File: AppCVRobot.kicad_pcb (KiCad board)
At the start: 2 copper layers, 34 parts, among them U1 LevelShifter

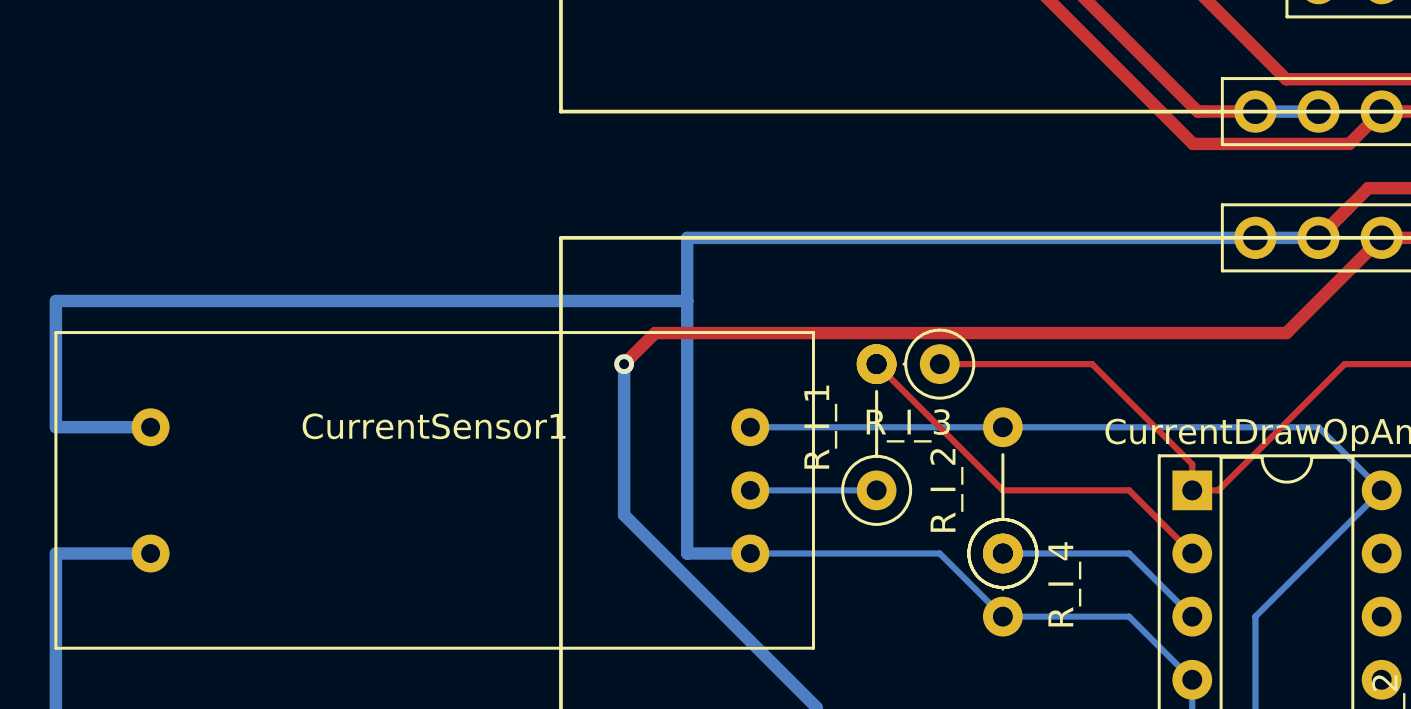
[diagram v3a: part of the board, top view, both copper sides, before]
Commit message: Added power switch connector
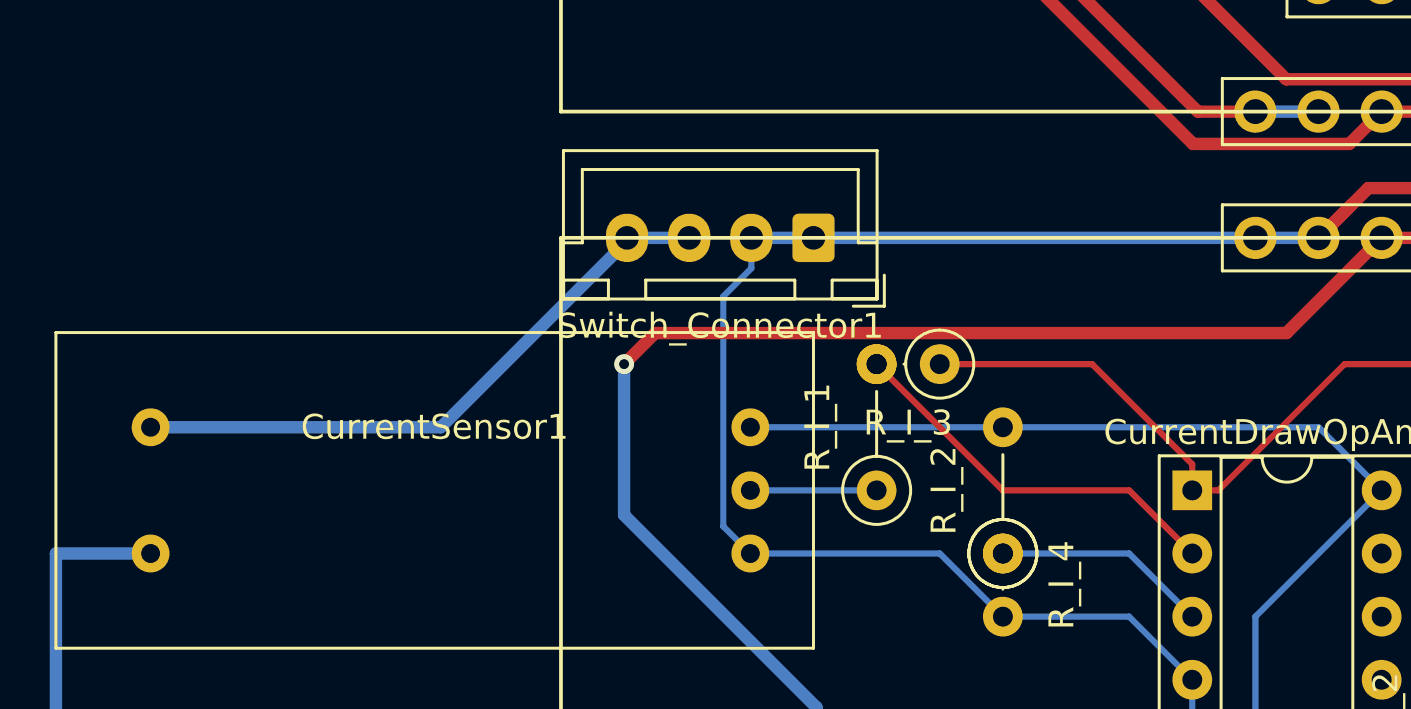
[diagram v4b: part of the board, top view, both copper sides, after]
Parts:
- added Switch_Connector1: Conn_01x04, Connector_JST:JST_XH_B4B-XH-A_1x04_P2.50mm_Vertical, F.Cu at (139.7, 78.7)
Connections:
- CurrentSensor1 pad 5: GND -> Net-(CurrentSensor1-Pad5)
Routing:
- net GND: track 386.2 -> 347.7 mm
- net Net-(CurrentSensor1-Pad5): track 0.00 -> 24.9 mm
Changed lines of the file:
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@@
     (thickness 1.6)
     (drawings 8)
-    (tracks 286)
+    (tracks 289)
     (zones 0)
-    (modules 34)
-    (nets 63)
+    (modules 35)
+    (nets 64)
   )
   (page A4)
@@
   (net 61 "Net-(Display_Connector1-Pad4)")
   (net 62 "Net-(Display_Connector1-Pad3)")
+  (net 63 "Net-(CurrentSensor1-Pad5)")
   (net_class Default "This is the default net class."
     (clearance 0.2)
@@
     (add_net "Net-(CurrentDrawOpAmp1-Pad3)")
     (add_net "Net-(CurrentSensor1-Pad2)")
+    (add_net "Net-(CurrentSensor1-Pad5)")
     (add_net "Net-(Display_Connector1-Pad3)")
     (add_net "Net-(Display_Connector1-Pad4)")
@@
     (add_net Step_L)
     (add_net Step_R)
+  )
+  (module Connector_JST:JST_XH_B4B-XH-A_1x04_P2.50mm_Vertical (layer F.Cu)
+    (at 139.7 78.74 180)
+    (descr "JST XH series connector, B4B-XH-A (http://www.jst-mfg.com/product/pdf/eng/eXH.pdf), generated with kicad-footprint-generator")
+    (tags "connector JST XH vertical")
+    (fp_text reference Switch_Connector1 (at 3.75 -3.55) (layer F.SilkS)
+      (effects (font (size 1 1) (thickness 0.15)))
+    )
+    (fp_text value Conn_01x04 (at 3.75 4.6) (layer F.Fab)
+      (effects (font (size 1 1) (thickness 0.15)))
+    )
+    (fp_text user %R (at 3.75 2.7) (layer F.Fab)
+      (effects (font (size 1 1) (thickness 0.15)))
+    )
+    (fp_line (start -2.85 -2.75) (end -2.85 -1.5) (layer F.SilkS) (width 0.12))
+    (fp_line (start -1.6 -2.75) (end -2.85 -2.75) (layer F.SilkS) (width 0.12))
+    (fp_line (start 9.3 2.75) (end 3.75 2.75) (layer F.SilkS) (width 0.12))
+    (fp_line (start 9.3 -0.2) (end 9.3 2.75) (layer F.SilkS) (width 0.12))
+    (fp_line (start 10.05 -0.2) (end 9.3 -0.2) (layer F.SilkS) (width 0.12))
+    (fp_line (start -1.8 2.75) (end 3.75 2.75) (layer F.SilkS) (width 0.12))
+    (fp_line (start -1.8 -0.2) (end -1.8 2.75) (layer F.SilkS) (width 0.12))
+    (fp_line (start -2.55 -0.2) (end -1.8 -0.2) (layer F.SilkS) (width 0.12))
+    (fp_line (start 10.05 -2.45) (end 8.25 -2.45) (layer F.SilkS) (width 0.12))
+    (fp_line (start 10.05 -1.7) (end 10.05 -2.45) (layer F.SilkS) (width 0.12))
+    (fp_line (start 8.25 -1.7) (end 10.05 -1.7) (layer F.SilkS) (width 0.12))
+    (fp_line (start 8.25 -2.45) (end 8.25 -1.7) (layer F.SilkS) (width 0.12))
+    (fp_line (start -0.75 -2.45) (end -2.55 -2.45) (layer F.SilkS) (width 0.12))
+    (fp_line (start -0.75 -1.7) (end -0.75 -2.45) (layer F.SilkS) (width 0.12))
+    (fp_line (start -2.55 -1.7) (end -0.75 -1.7) (layer F.SilkS) (width 0.12))
+    (fp_line (start -2.55 -2.45) (end -2.55 -1.7) (layer F.SilkS) (width 0.12))
+    (fp_line (start 6.75 -2.45) (end 0.75 -2.45) (layer F.SilkS) (width 0.12))
+    (fp_line (start 6.75 -1.7) (end 6.75 -2.45) (layer F.SilkS) (width 0.12))
+    (fp_line (start 0.75 -1.7) (end 6.75 -1.7) (layer F.SilkS) (width 0.12))
+    (fp_line (start 0.75 -2.45) (end 0.75 -1.7) (layer F.SilkS) (width 0.12))
+    (fp_line (start 0 -1.35) (end 0.625 -2.35) (layer F.Fab) (width 0.1))
+    (fp_line (start -0.625 -2.35) (end 0 -1.35) (layer F.Fab) (width 0.1))
+    (fp_line (start 10.45 -2.85) (end -2.95 -2.85) (layer F.CrtYd) (width 0.05))
+    (fp_line (start 10.45 3.9) (end 10.45 -2.85) (layer F.CrtYd) (width 0.05))
+    (fp_line (start -2.95 3.9) (end 10.45 3.9) (layer F.CrtYd) (width 0.05))
+    (fp_line (start -2.95 -2.85) (end -2.95 3.9) (layer F.CrtYd) (width 0.05))
+    (fp_line (start 10.06 -2.46) (end -2.56 -2.46) (layer F.SilkS) (width 0.12))
+    (fp_line (start 10.06 3.51) (end 10.06 -2.46) (layer F.SilkS) (width 0.12))
+    (fp_line (start -2.56 3.51) (end 10.06 3.51) (layer F.SilkS) (width 0.12))
+    (fp_line (start -2.56 -2.46) (end -2.56 3.51) (layer F.SilkS) (width 0.12))
+    (fp_line (start 9.95 -2.35) (end -2.45 -2.35) (layer F.Fab) (width 0.1))
+    (fp_line (start 9.95 3.4) (end 9.95 -2.35) (layer F.Fab) (width 0.1))
+    (fp_line (start -2.45 3.4) (end 9.95 3.4) (layer F.Fab) (width 0.1))
+    (fp_line (start -2.45 -2.35) (end -2.45 3.4) (layer F.Fab) (width 0.1))
+    (pad 4 thru_hole oval (at 7.5 0 180) (size 1.7 1.95) (drill 0.95) (layers *.Cu *.Mask)
+      (net 63 "Net-(CurrentSensor1-Pad5)"))
+    (pad 3 thru_hole oval (at 5 0 180) (size 1.7 1.95) (drill 0.95) (layers *.Cu *.Mask)
+      (net 63 "Net-(CurrentSensor1-Pad5)"))
+    (pad 2 thru_hole oval (at 2.5 0 180) (size 1.7 1.95) (drill 0.95) (layers *.Cu *.Mask)
+      (net 8 GND))
+    (pad 1 thru_hole roundrect (at 0 0 180) (size 1.7 1.95) (drill 0.95) (layers *.Cu *.Mask) (roundrect_rratio 0.147059)
+      (net 8 GND))
+    (model ${KISYS3DMOD}/Connector_JST.3dshapes/JST_XH_B4B-XH-A_1x04_P2.50mm_Vertical.wrl
+      (at (xyz 0 0 0))
+      (scale (xyz 1 1 1))
+      (rotate (xyz 0 0 0))
+    )
   )
   (module CustomFootprints:LevelShifterBreakoutBoard (layer F.Cu)
@@
     (fp_line (start 15.24 6.35) (end 15.24 -6.35) (layer F.SilkS) (width 0.12))
     (pad 5 thru_hole circle (at -11.43 -2.54 180) (size 1.524 1.524) (drill 0.762) (layers *.Cu *.Mask)
-      (net 8 GND))
+      (net 63 "Net-(CurrentSensor1-Pad5)"))
     (pad 4 thru_hole circle (at -11.43 2.54 180) (size 1.524 1.524) (drill 0.762) (layers *.Cu *.Mask)
       (net 27 "Net-(Battery_Connector1-Pad5)"))
@@
   (segment (start 143.51 49.903965) (end 137.699989 44.093954) (width 0.5) (layer F.Cu) (net 3))
   (segment (start 143.51 57.15) (end 143.51 49.903965) (width 0.5) (layer F.Cu) (net 3))
+  (segment (start 139.82 101.6) (end 139.82 101.475) (width 0.25) (layer F.Cu) (net 3))
+  (segment (start 142.32 101.475) (end 142.32 101.6) (width 0.25) (layer F.Cu) (net 3))
+  (segment (start 132.08 89.889963) (end 132.08 83.82) (width 0.5) (layer B.Cu) (net 3))
+  (segment (start 139.82 101.6) (end 139.82 97.629963) (width 0.5) (layer B.Cu) (net 3))
+  (segment (start 139.82 97.629963) (end 132.08 89.889963) (width 0.5) (layer B.Cu) (net 3))
+  (segment (start 142.32 101.6) (end 139.82 101.6) (width 0.5) (layer B.Cu) (net 3))
   (segment (start 144.78 38.1) (end 154.94 48.26) (width 0.25) (layer B.Cu) (net 4))
   (segment (start 142.24 38.1) (end 144.78 38.1) (width 0.25) (layer B.Cu) (net 4))
@@
   (segment (start 172.72 96.52) (end 172.72 101.56) (width 0.25) (layer B.Cu) (net 8))
   (segment (start 160.02 78.74) (end 157.48 78.74) (width 0.5) (layer B.Cu) (net 8))
-  (segment (start 157.48 78.74) (end 134.62 78.74) (width 0.5) (layer B.Cu) (net 8))
-  (segment (start 134.62 91.44) (end 137.16 91.44) (width 0.5) (layer B.Cu) (net 8))
-  (segment (start 134.62 81.28) (end 109.22 81.28) (width 0.5) (layer B.Cu) (net 8))
-  (segment (start 134.62 81.28) (end 134.62 91.44) (width 0.5) (layer B.Cu) (net 8))
-  (segment (start 134.62 78.74) (end 134.62 81.28) (width 0.5) (layer B.Cu) (net 8))
-  (segment (start 109.22 81.28) (end 109.22 86.36) (width 0.5) (layer B.Cu) (net 8))
-  (segment (start 109.22 86.36) (end 113.03 86.36) (width 0.5) (layer B.Cu) (net 8))
   (segment (start 160.02 78.74) (end 161.320001 77.439999) (width 0.5) (layer F.Cu) (net 8))
   (segment (start 182.8 86.28) (end 180.34 83.82) (width 0.25) (layer B.Cu) (net 8))
@@
   (segment (start 135.89 59.69) (end 135.89 50.595) (width 0.25) (layer F.Cu) (net 8))
   (segment (start 140.97 59.69) (end 135.89 59.69) (width 0.25) (layer F.Cu) (net 8))
+  (segment (start 137.2 78.74) (end 139.7 78.74) (width 0.5) (layer B.Cu) (net 8))
+  (segment (start 139.7 78.74) (end 157.48 78.74) (width 0.5) (layer B.Cu) (net 8))
+  (segment (start 137.2 79.965) (end 137.2 78.74) (width 0.25) (layer B.Cu) (net 8))
+  (segment (start 136.072999 81.092001) (end 137.2 79.965) (width 0.25) (layer B.Cu) (net 8))
+  (segment (start 136.072999 90.352999) (end 136.072999 81.092001) (width 0.25) (layer B.Cu) (net 8))
+  (segment (start 137.16 91.44) (end 136.072999 90.352999) (width 0.25) (layer B.Cu) (net 8))
   (segment (start 167.64 53.34) (end 167.64 50.8) (width 0.25) (layer B.Cu) (net 9))
   (segment (start 167.64 50.8) (end 165.1 48.26) (width 0.25) (layer B.Cu) (net 9))
@@
   (segment (start 163.685001 97.934999) (end 166.840001 94.779999) (width 0.25) (layer F.Cu) (net 15))
   (segment (start 166.840001 94.779999) (end 167.64 93.98) (width 0.25) (layer F.Cu) (net 15))
-  (segment (start 139.82 101.6) (end 139.82 101.475) (width 0.25) (layer F.Cu) (net 3))
-  (segment (start 142.32 101.475) (end 142.32 101.6) (width 0.25) (layer F.Cu) (net 3))
-  (segment (start 132.08 89.889963) (end 132.08 83.82) (width 0.5) (layer B.Cu) (net 3))
-  (segment (start 139.82 101.6) (end 139.82 97.629963) (width 0.5) (layer B.Cu) (net 3))
-  (segment (start 139.82 97.629963) (end 132.08 89.889963) (width 0.5) (layer B.Cu) (net 3))
-  (segment (start 142.32 101.6) (end 139.82 101.6) (width 0.5) (layer B.Cu) (net 3))
   (segment (start 148.360001 97.934999) (end 163.685001 97.934999) (width 0.25) (layer F.Cu) (net 15))
   (segment (start 144.82 101.475) (end 148.360001 97.934999) (width 0.25) (layer F.Cu) (net 15))
@@
   (segment (start 129.722999 46.642001) (end 131.955 44.41) (width 0.25) (layer F.Cu) (net 62))
   (segment (start 130.81 64.77) (end 129.722999 63.682999) (width 0.25) (layer F.Cu) (net 62))
+  (segment (start 132.2 78.865) (end 132.2 78.74) (width 0.5) (layer B.Cu) (net 63))
+  (segment (start 124.705 86.36) (end 132.2 78.865) (width 0.5) (layer B.Cu) (net 63))
+  (segment (start 113.03 86.36) (end 124.705 86.36) (width 0.5) (layer B.Cu) (net 63))
+  (segment (start 132.2 78.74) (end 134.7 78.74) (width 0.5) (layer B.Cu) (net 63))
 )

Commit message: main changes
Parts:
- removed Jumper_Motor_Step1: Conn_01x06_Male, Connector_PinHeader_2.54mm:PinHeader_2x03_P2.54mm_Vertical
- added Diode1: D, Diode_THT:D_T-1_P5.08mm_Horizontal, F.Cu at (189.2, 76.2)
- added Q1: TIP120, Package_TO_SOT_THT:TO-220-3_Vertical, F.Cu at (195.6, 99.1)
- added RV1: R_POT_TRIM, Potentiometer_THT:Potentiometer_Bourns_3296W_Vertical, F.Cu at (195.6, 81.3)
- added R_T1: 1K, Resistor_THT:R_Axial_DIN0207_L6.3mm_D2.5mm_P5.08mm_Vertical, F.Cu at (194.3, 83.8)
- Con_MainBoard2PowerBoard1: footprint Connector_PinSocket_2.54mm:PinSocket_1x09_P2.54mm_Vertical -> Connector_PinSocket_2.54mm:PinSocket_1x11_P2.54mm_Vertical
- Con_PowerBoard2MainBoard1: footprint Connector_PinHeader_2.54mm:PinHeader_1x09_P2.54mm_Vertical -> Connector_PinHeader_2.54mm:PinHeader_1x11_P2.54mm_Vertical
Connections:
- Con_MainBoard2PowerBoard1 pad 1: Net-(Con_MainBoard2PowerBoard1-Pad1) -> PCheck
- Con_MainBoard2PowerBoard1 pad 2: Net-(Con_MainBoard2PowerBoard1-Pad2) -> PowerIN
- Con_MainBoard2PowerBoard1 pad 5: +5V -> Net-(Con_MainBoard2PowerBoard1-Pad5)
- Con_MainBoard2PowerBoard1 pad 6: +BATT -> Net-(Con_MainBoard2PowerBoard1-Pad6)
- Con_MainBoard2PowerBoard1 pad 7: +BATT -> +5V
- Con_MainBoard2PowerBoard1 pad 8: GND -> +BATT
- Con_MainBoard2PowerBoard1 pad 9: GND -> +BATT
- Con_PowerBoard2MainBoard1 pad 1: Net-(Con_PowerBoard2MainBoard1-Pad1) -> P_Check
- Con_PowerBoard2MainBoard1 pad 2: Net-(CellVoltageOpAmp1-Pad7) -> P_IN
- Con_PowerBoard2MainBoard1 pad 3: Net-(CellVoltageOpAmp1-Pad1) -> Net-(Con_PowerBoard2MainBoard1-Pad3)
- Con_PowerBoard2MainBoard1 pad 4: Net-(Con_PowerBoard2MainBoard1-Pad4) -> Net-(CellVoltageOpAmp1-Pad7)
- Con_PowerBoard2MainBoard1 pad 5: +5V -> Net-(CellVoltageOpAmp1-Pad1)
- Con_PowerBoard2MainBoard1 pad 6: +BATT -> Net-(Con_PowerBoard2MainBoard1-Pad6)
- Con_PowerBoard2MainBoard1 pad 7: +BATT -> +5V
- Con_PowerBoard2MainBoard1 pad 8: GND -> +BATT
- Con_PowerBoard2MainBoard1 pad 9: GND -> +BATT
- Con_Stepdown_Board1 pad 3: GND -> Net-(Con_Stepdown_Board1-Pad3)
- CurrentDrawOpAmp1 pad 1: Net-(Con_PowerBoard2MainBoard1-Pad4) -> Net-(Con_PowerBoard2MainBoard1-Pad6)
- MD_L1 pad 10: MS1 -> MS1_L
- MD_L1 pad 11: MS2 -> MS2_L
- MD_L1 pad 12: MS3 -> MS3_L
- MD_R1 pad 10: MS1 -> MS1_R
- MD_R1 pad 11: MS2 -> MS2_R
- MD_R1 pad 12: MS3 -> MS3_R
- MicroController1 pad 13: Net-(MicroController1-Pad13) -> MS1_L
- MicroController1 pad 14: Net-(MicroController1-Pad14) -> MS2_L
- MicroController1 pad 15: Net-(MicroController1-Pad15) -> MS3_L
- MicroController1 pad 17: Net-(MicroController1-Pad17) -> PowerIN
- MicroController1 pad 18: Net-(MicroController1-Pad18) -> PCheck
- MicroController1 pad 19: Net-(Con_MainBoard2PowerBoard1-Pad4) -> Net-(Con_MainBoard2PowerBoard1-Pad6)
- MicroController1 pad 20: Net-(Con_MainBoard2PowerBoard1-Pad3) -> Net-(Con_MainBoard2PowerBoard1-Pad5)
- MicroController1 pad 21: Net-(Con_MainBoard2PowerBoard1-Pad2) -> Net-(Con_MainBoard2PowerBoard1-Pad4)
- MicroController1 pad 23: Net-(Con_MainBoard2PowerBoard1-Pad1) -> Net-(Con_MainBoard2PowerBoard1-Pad3)
- MicroController1 pad 6: Net-(MicroController1-Pad6) -> MS3_R
- MicroController1 pad 7: Net-(MicroController1-Pad7) -> MS2_R
- MicroController1 pad 8: Net-(MicroController1-Pad8) -> MS1_R
- R_Cell1_Vdiv_A1 pad 2: Net-(Con_PowerBoard2MainBoard1-Pad1) -> Net-(Con_PowerBoard2MainBoard1-Pad3)
- R_Cell1_Vdiv_B1 pad 1: Net-(Con_PowerBoard2MainBoard1-Pad1) -> Net-(Con_PowerBoard2MainBoard1-Pad3)
- R_I_3 pad 1: Net-(Con_PowerBoard2MainBoard1-Pad4) -> Net-(Con_PowerBoard2MainBoard1-Pad6)
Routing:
- net MS3: track 56.7 -> 0.00 mm, vias 1 -> 0
- net MS2: track 49.5 -> 0.00 mm, vias 1 -> 0
- net MS1: track 42.3 -> 0.00 mm, vias 1 -> 0
- net GND: track 347.7 -> 305.7 mm
- net Net-(Con_PowerBoard2MainBoard1-Pad4): track 33.8 -> 0.00 mm, vias 1 -> 0
- net Net-(Con_PowerBoard2MainBoard1-Pad6): track 0.00 -> 33.8 mm, vias 0 -> 1
- net MS3_L: track 0.00 -> 29.0 mm
- net MS2_L: track 0.00 -> 28.2 mm
- net MS1_L: track 0.00 -> 24.5 mm
- net Net-(Con_Stepdown_Board1-Pad3): track 0.00 -> 22.3 mm
- net PCheck: track 0.00 -> 22.0 mm
- net +BATT: track 208.1 -> 229.7 mm
- net P_Check: track 0.00 -> 15.3 mm
- net Net-(Q1-Pad1): track 0.00 -> 11.8 mm
- net P_IN: track 0.00 -> 9.94 mm
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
